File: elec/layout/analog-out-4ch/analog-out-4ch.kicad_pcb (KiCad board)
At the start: 2 copper layers, 15 parts, among them U1 100Ω ±1% 62.5mW, U10 100nF ±10% 16V X7R, U2 100Ω ±1% 62.5mW, U3 100Ω ±1% 62.5mW, U4 100Ω ±1% 62.5mW, U5 100Ω ±1% 62.5mW, U6 100Ω ±1% 62.5mW, U7 100Ω ±1% 62.5mW, U8 100Ω ±1% 62.5mW

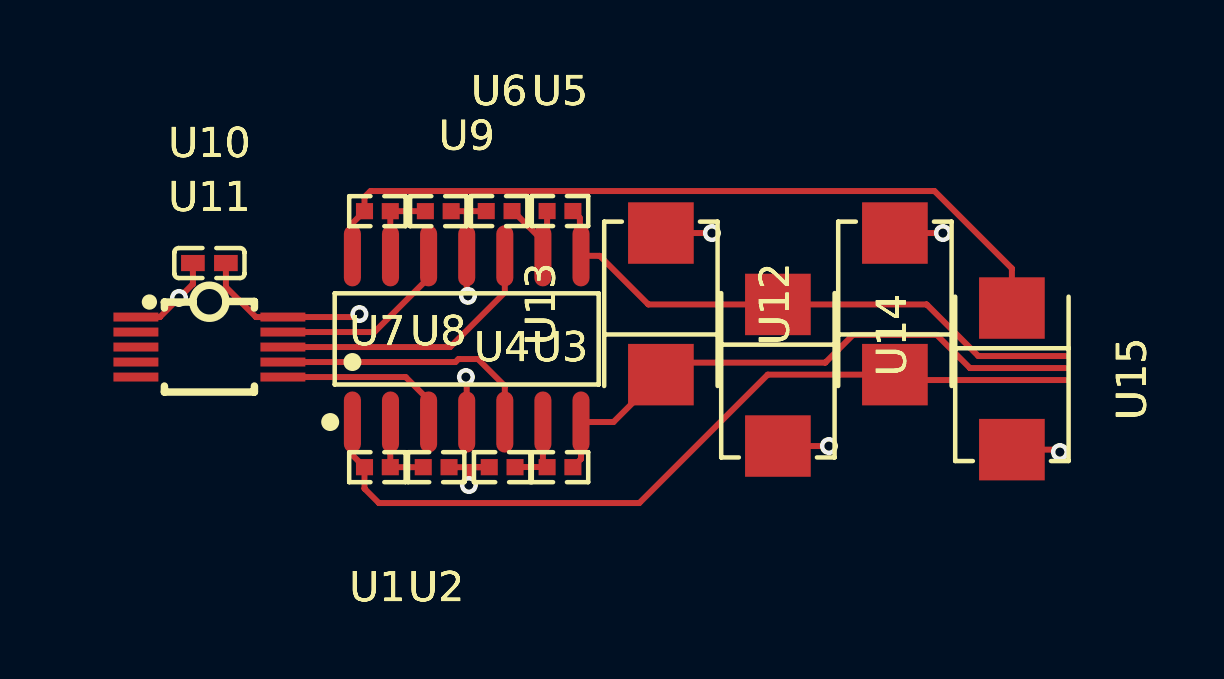
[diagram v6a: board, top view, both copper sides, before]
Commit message: add pretty outline
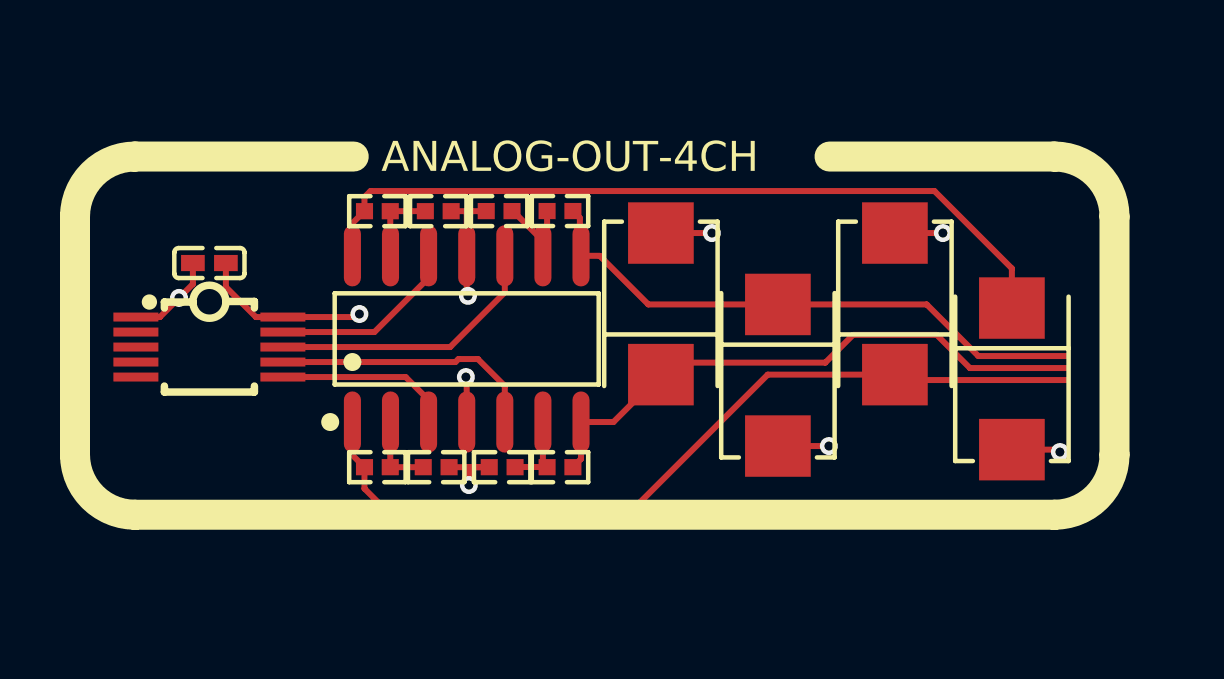
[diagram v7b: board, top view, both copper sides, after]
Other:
- board text added: "ANALOG-OUT-4CH"

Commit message: building frozen
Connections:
- net line-4 renamed IN3plus
- net line-5 renamed IN2plus
- net line-7 renamed SCL
- net line-8 renamed VOUTD
- net line-9 renamed SDA
- U1 pad 2: line-6 -> line-2
- U10 pad 1: hv-1 -> hv
- U11 pad 1: hv-1 -> hv
- U11 pad 6: line -> IN1plus
- U12 pad 1: line-6 -> line-2
- U14 pad 1: line-2 -> line-3
- U15 pad 1: line-3 -> line
- U5 pad 2: line-2 -> line-3
- U7 pad 2: line-3 -> line
- U9 pad 1: line-6 -> line-2
- U9 pad 14: line-3 -> line
- U9 pad 3: line -> IN1plus
- U9 pad 4: hv -> hv-1
- U9 pad 8: line-2 -> line-3
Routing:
- net line-6: track 28.3 -> 0.00 mm
- net line: track 5.91 -> 26.7 mm
- net line-2: track 19.2 -> 28.3 mm
- net line-3: track 26.7 -> 19.2 mm
- net IN1plus: track 0.00 -> 5.91 mm
- net hv-1: track 3.06 -> 1.51 mm
- net hv: track 1.51 -> 3.06 mm
